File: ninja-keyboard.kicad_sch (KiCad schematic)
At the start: 154 parts, among them J1 USB_C_Receptacle_USB2.0_14P, J2 Conn_01x02, J3 Conn_01x05_Pin, Q1 AO3401A, Q2 SS8050, SW1 backquote, SW10 num9, SW11 num0, SW12 -, SW13 =, SW14 backsapce, SW15 tab, SW16 q, SW17 w, SW18 e, SW19 r, SW2 num1, SW20 t, SW21 y, SW22 u, SW23 i, SW24 o, SW25 p, SW26 [, SW27 ], SW28 \, SW29 cap, SW3 num2, SW30 a, SW31 s, SW32 d, SW33 f, SW34 h, SW35 g, SW36 j, SW37 k, SW38 l, SW39 semicolon, SW4 num3, SW40 apostrophe, SW41 enter, SW42 pgdown, SW43 lshift, SW44 z, SW45 x, SW46 c, SW47 v, SW48 b, SW49 n, SW5 num4, SW50 m, SW51 comma, SW52 period, SW53 /, SW54 rshift, SW55 up, SW56 end, SW57 lctrl, SW58 win, SW59 lalt, SW6 num5, SW60 lfn, SW61 space, SW62 macro, SW63 rfn, SW64 ralt, SW65 rctrl, SW66 left, SW67 down, SW68 right, SW69 pgup, SW7 num6, SW70 home, SW71 RotaryEncoder, SW72 SW_SPDT, SW8 num7, SW9 num8, U1 ESP32-S3-WROOM-1, U3 TP4056-42-ESOP8

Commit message: Seperate capacitors and LEDs from the mechanical keys
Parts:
- added C1, C10, C11, C12, C13, C14, C15, C16, C17, C18, C19, C2, C20, C21, C22, C23, C24, C25, C26, C27, C28, C29, C3, C30, C31, C32, C33, C34, C35, C36, C37, C38, C39, C4, C40, C41, C42, C43, C44, C45, C46, C47, C48, C49, C5, C50, C51, C52, C53, C54, C55, C56, C57, C58, C59, C6, C60, C61, C62, C63, C64, C65, C66, C67, C68, C69, C7, C70, C8, C9: 0.1uF, Capacitor_SMD:C_0603_1608Metric, symbol Device:C_Small
- added SL1, SL10, SL11, SL12, SL13, SL14, SL15, SL16, SL17, SL18, SL19, SL2, SL20, SL21, SL22, SL23, SL24, SL25, SL26, SL27, SL28, SL29, SL3, SL30, SL31, SL32, SL33, SL34, SL35, SL36, SL37, SL38, SL39, SL4, SL40, SL41, SL42, SL43, SL44, SL45, SL46, SL47, SL48, SL49, SL5, SL50, SL51, SL52, SL53, SL54, SL55, SL56, SL57, SL58, SL59, SL6, SL60, SL61, SL62, SL63, SL64, SL65, SL66, SL67, SL68, SL69, SL7, SL70, SL8, SL9: Smart LED, user_added:Smart LED 6028, symbol user_created:Smart LED
- SW1, SW10, SW11, SW12, SW13, SW16, SW17, SW18, SW19, SW2, SW20, SW21, SW22, SW23, SW24, SW25, SW26, SW27, SW3, SW30, SW31, SW32, SW33, SW34, SW35, SW36, SW37, SW38, SW39, SW4, SW40, SW42, SW44, SW45, SW46, SW47, SW48, SW49, SW5, SW50, SW51, SW52, SW53, SW55, SW56, SW6, SW60, SW63, SW66, SW67, SW68, SW69, SW7, SW70, SW8, SW9: footprint user_added:SW_Hotswap_Kailh_MX_1.00u with led -> PCM_Switch_Keyboard_Hotswap_Kailh:SW_Hotswap_Kailh_MX_1.00u; symbol user_created:SW_Push with Smart LED -> Switch:SW_Push
- SW14, SW29: footprint user_added:SW_Hotswap_Kailh_MX_1.75u with led -> PCM_Switch_Keyboard_Hotswap_Kailh:SW_Hotswap_Kailh_MX_1.75u; symbol user_created:SW_Push with Smart LED -> Switch:SW_Push
- SW15: footprint user_added:SW_Hotswap_Kailh_MX_1.50u with led -> PCM_Switch_Keyboard_Hotswap_Kailh:SW_Hotswap_Kailh_MX_1.50u; symbol user_created:SW_Push with Smart LED -> Switch:SW_Push
- SW28, SW57, SW58, SW59, SW64, SW65: footprint user_added:SW_Hotswap_Kailh_MX_1.25u with led -> PCM_Switch_Keyboard_Hotswap_Kailh:SW_Hotswap_Kailh_MX_1.25u; symbol user_created:SW_Push with Smart LED -> Switch:SW_Push
- SW41: footprint user_added:SW_Hotswap_Kailh_MX_2.00u with led -> PCM_Switch_Keyboard_Hotswap_Kailh:SW_Hotswap_Kailh_MX_2.00u; symbol user_created:SW_Push with Smart LED -> Switch:SW_Push
- SW43, SW61, SW62: footprint user_added:SW_Hotswap_Kailh_MX_2.25u with led -> PCM_Switch_Keyboard_Hotswap_Kailh:SW_Hotswap_Kailh_MX_2.25u; symbol user_created:SW_Push with Smart LED -> Switch:SW_Push
- SW54: footprint user_added:SW_Hotswap_Kailh_MX_1.50u with led -> PCM_Switch_Keyboard_Hotswap_Kailh:SW_Hotswap_Kailh_MX_1.00u; symbol user_created:SW_Push with Smart LED -> Switch:SW_Push
- renumbered C3 to C71, C4 to C72, C11 to C73, C5 to C74, C1 to C75, C2 to C76, C6 to C77, C7 to C78, C8 to C79, C9 to C80, C10 to C81, D38 to D36, D36 to D37, D37 to D38, J3 to J1, J4 to J2, J1 to J3, J2 to J4, Q2 to Q1, Q1 to Q2, R18 to R1, R9 to R11, R11 to R12, R12 to R13, R6 to R14, R3 to R15, R4 to R16, R8 to R17, R5 to R18, R14 to R19, R21 to R2, R16 to R20, R15 to R21, R17 to R22, R13 to R23, R1 to R3, R22 to R4, R23 to R5, R7 to R6, R2 to R7, R19 to R8, R20 to R9, U3 to U2, U2 to U3
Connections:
- net 3V3: now also C1.1, C10.1, C11.1, C12.1, C13.1, C14.1, C15.1, C16.1, C17.1, C18.1, C19.1, C2.1, C20.1, C21.1, C22.1, C23.1, C24.1, C25.1, C26.1, C27.1, C28.1, C29.1, C3.1, C30.1, C31.1, C32.1, C33.1, C34.1, C35.1, C36.1, C37.1, C38.1, C39.1, C4.1, C40.1, C41.1, C42.1, C43.1, C44.1, C45.1, C46.1, C47.1, C48.1, C49.1, C5.1, C50.1, C51.1, C52.1, C53.1, C54.1, C55.1, C56.1, C57.1, C58.1, C59.1, C6.1, C60.1, C61.1, C62.1, C63.1, C64.1, C65.1, C66.1, C67.1, C68.1, C69.1, C7.1, C70.1, C8.1, C9.1, SL1.1 (VDD), SL10.1 (VDD), SL11.1 (VDD), SL12.1 (VDD), SL13.1 (VDD), SL14.1 (VDD), SL15.1 (VDD), SL16.1 (VDD), SL17.1 (VDD), SL18.1 (VDD), SL19.1 (VDD), SL2.1 (VDD), SL20.1 (VDD), SL21.1 (VDD), SL22.1 (VDD), SL23.1 (VDD), SL24.1 (VDD), SL25.1 (VDD), SL26.1 (VDD), SL27.1 (VDD), SL28.1 (VDD), SL29.1 (VDD), SL3.1 (VDD), SL30.1 (VDD), SL31.1 (VDD), SL32.1 (VDD), SL33.1 (VDD), SL34.1 (VDD), SL35.1 (VDD), SL36.1 (VDD), SL37.1 (VDD), SL38.1 (VDD), SL39.1 (VDD), SL4.1 (VDD), SL40.1 (VDD), SL41.1 (VDD), SL42.1 (VDD), SL43.1 (VDD), SL44.1 (VDD), SL45.1 (VDD), SL46.1 (VDD), SL47.1 (VDD), SL48.1 (VDD), SL49.1 (VDD), SL5.1 (VDD), SL50.1 (VDD), SL51.1 (VDD), SL52.1 (VDD), SL53.1 (VDD), SL54.1 (VDD), SL55.1 (VDD), SL56.1 (VDD), SL57.1 (VDD), SL58.1 (VDD), SL59.1 (VDD), SL6.1 (VDD), SL60.1 (VDD), SL61.1 (VDD), SL62.1 (VDD), SL63.1 (VDD), SL64.1 (VDD), SL65.1 (VDD), SL66.1 (VDD), SL67.1 (VDD), SL68.1 (VDD), SL69.1 (VDD), SL7.1 (VDD), SL70.1 (VDD), SL8.1 (VDD), SL9.1 (VDD); no longer SW1.3 (VDD), SW10.3 (VDD), SW11.3 (VDD), SW12.3 (VDD), SW13.3 (VDD), SW14.3 (VDD), SW15.3 (VDD), SW16.3 (VDD), SW17.3 (VDD), SW18.3 (VDD), SW19.3 (VDD), SW2.3 (VDD), SW20.3 (VDD), SW21.3 (VDD), SW22.3 (VDD), SW23.3 (VDD), SW24.3 (VDD), SW25.3 (VDD), SW26.3 (VDD), SW27.3 (VDD), SW28.3 (VDD), SW29.3 (VDD), SW3.3 (VDD), SW30.3 (VDD), SW31.3 (VDD), SW32.3 (VDD), SW33.3 (VDD), SW34.3 (VDD), SW35.3 (VDD), SW36.3 (VDD), SW37.3 (VDD), SW38.3 (VDD), SW39.3 (VDD), SW4.3 (VDD), SW40.3 (VDD), SW41.3 (VDD), SW42.3 (VDD), SW43.3 (VDD), SW44.3 (VDD), SW45.3 (VDD), SW46.3 (VDD), SW47.3 (VDD), SW48.3 (VDD), SW49.3 (VDD), SW5.3 (VDD), SW50.3 (VDD), SW51.3 (VDD), SW52.3 (VDD), SW53.3 (VDD), SW54.3 (VDD), SW55.3 (VDD), SW56.3 (VDD), SW57.3 (VDD), SW58.3 (VDD), SW59.3 (VDD), SW6.3 (VDD), SW60.3 (VDD), SW61.3 (VDD), SW62.3 (VDD), SW63.3 (VDD), SW64.3 (VDD), SW65.3 (VDD), SW66.3 (VDD), SW67.3 (VDD), SW68.3 (VDD), SW69.3 (VDD), SW7.3 (VDD), SW70.3 (VDD), SW8.3 (VDD), SW9.3 (VDD)
- net GND: now also C1.2, C10.2, C11.2, C12.2, C13.2, C14.2, C15.2, C16.2, C17.2, C18.2, C19.2, C2.2, C20.2, C21.2, C22.2, C23.2, C24.2, C25.2, C26.2, C27.2, C28.2, C29.2, C3.2, C30.2, C31.2, C32.2, C33.2, C34.2, C35.2, C36.2, C37.2, C38.2, C39.2, C4.2, C40.2, C41.2, C42.2, C43.2, C44.2, C45.2, C46.2, C47.2, C48.2, C49.2, C5.2, C50.2, C51.2, C52.2, C53.2, C54.2, C55.2, C56.2, C57.2, C58.2, C59.2, C6.2, C60.2, C61.2, C62.2, C63.2, C64.2, C65.2, C66.2, C67.2, C68.2, C69.2, C7.2, C70.2, C8.2, C9.2, SL1.4 (GND), SL10.4 (GND), SL11.4 (GND), SL12.4 (GND), SL13.4 (GND), SL14.4 (GND), SL15.4 (GND), SL16.4 (GND), SL17.4 (GND), SL18.4 (GND), SL19.4 (GND), SL2.4 (GND), SL20.4 (GND), SL21.4 (GND), SL22.4 (GND), SL23.4 (GND), SL24.4 (GND), SL25.4 (GND), SL26.4 (GND), SL27.4 (GND), SL28.4 (GND), SL29.4 (GND), SL3.4 (GND), SL30.4 (GND), SL31.4 (GND), SL32.4 (GND), SL33.4 (GND), SL34.4 (GND), SL35.4 (GND), SL36.4 (GND), SL37.4 (GND), SL38.4 (GND), SL39.4 (GND), SL4.4 (GND), SL40.4 (GND), SL41.4 (GND), SL42.4 (GND), SL43.4 (GND), SL44.4 (GND), SL45.4 (GND), SL46.4 (GND), SL47.4 (GND), SL48.4 (GND), SL49.4 (GND), SL5.4 (GND), SL50.4 (GND), SL51.4 (GND), SL52.4 (GND), SL53.4 (GND), SL54.4 (GND), SL55.4 (GND), SL56.4 (GND), SL57.4 (GND), SL58.4 (GND), SL59.4 (GND), SL6.4 (GND), SL60.4 (GND), SL61.4 (GND), SL62.4 (GND), SL63.4 (GND), SL64.4 (GND), SL65.4 (GND), SL66.4 (GND), SL67.4 (GND), SL68.4 (GND), SL69.4 (GND), SL7.4 (GND), SL70.4 (GND), SL8.4 (GND), SL9.4 (GND); no longer SW1.6 (GND), SW10.6 (GND), SW11.6 (GND), SW12.6 (GND), SW13.6 (GND), SW14.6 (GND), SW15.6 (GND), SW16.6 (GND), SW17.6 (GND), SW18.6 (GND), SW19.6 (GND), SW2.6 (GND), SW20.6 (GND), SW21.6 (GND), SW22.6 (GND), SW23.6 (GND), SW24.6 (GND), SW25.6 (GND), SW26.6 (GND), SW27.6 (GND), SW28.6 (GND), SW29.6 (GND), SW3.6 (GND), SW30.6 (GND), SW31.6 (GND), SW32.6 (GND), SW33.6 (GND), SW34.6 (GND), SW35.6 (GND), SW36.6 (GND), SW37.6 (GND), SW38.6 (GND), SW39.6 (GND), SW4.6 (GND), SW40.6 (GND), SW41.6 (GND), SW42.6 (GND), SW43.6 (GND), SW44.6 (GND), SW45.6 (GND), SW46.6 (GND), SW47.6 (GND), SW48.6 (GND), SW49.6 (GND), SW5.6 (GND), SW50.6 (GND), SW51.6 (GND), SW52.6 (GND), SW53.6 (GND), SW54.6 (GND), SW55.6 (GND), SW56.6 (GND), SW57.6 (GND), SW58.6 (GND), SW59.6 (GND), SW6.6 (GND), SW60.6 (GND), SW61.6 (GND), SW62.6 (GND), SW63.6 (GND), SW64.6 (GND), SW65.6 (GND), SW66.6 (GND), SW67.6 (GND), SW68.6 (GND), SW69.6 (GND), SW7.6 (GND), SW70.6 (GND), SW8.6 (GND), SW9.6 (GND)
- net at R1.1: now also SL70.3 (DIN); no longer SW70.5 (DIN)
- new net: SL29.3 (DIN), SL30.2 (DOUT)
- new net: SL30.3 (DIN), SL31.2 (DOUT)
- new net: SL67.3 (DIN), SL68.2 (DOUT)
- new net: SL56.2 (DOUT), SL68.3 (DIN)
- new net: SL12.3 (DIN), SL13.2 (DOUT)
- new net: SL13.3 (DIN), SL14.2 (DOUT)
- new net: SL49.2 (DOUT), SL50.3 (DIN)
- new net: SL48.2 (DOUT), SL49.3 (DIN)
- new net: SL61.3 (DIN), SL62.2 (DOUT)
- new net: SL62.3 (DIN), SL63.2 (DOUT)
- new net: SL57.3 (DIN), SL58.2 (DOUT)
- new net: SL46.2 (DOUT), SL47.3 (DIN)
- new net: SL45.2 (DOUT), SL46.3 (DIN)
- new net: SL15.2 (DOUT), SL16.3 (DIN)
- new net: SL1.2 (DOUT), SL15.3 (DIN)
- new net: SL43.2 (DOUT), SL44.3 (DIN)
- new net: SL29.2 (DOUT), SL43.3 (DIN)
- new net: SL2.3 (DIN), SL3.2 (DOUT)
- new net: SL3.3 (DIN), SL4.2 (DOUT)
- new net: SL14.3 (DIN), SL70.2 (DOUT)
- new net: SL63.3 (DIN), SL64.2 (DOUT)
- new net: SL64.3 (DIN), SL65.2 (DOUT)
- new net: SL38.3 (DIN), SL39.2 (DOUT)
- new net: SL39.3 (DIN), SL40.2 (DOUT)
- new net: SL52.2 (DOUT), SL53.3 (DIN)
- new net: SL51.2 (DOUT), SL52.3 (DIN)
- new net: SL47.2 (DOUT), SL48.3 (DIN)
- new net: SL11.3 (DIN), SL12.2 (DOUT)
- new net: SL58.3 (DIN), SL59.2 (DOUT)
- new net: SL50.2 (DOUT), SL51.3 (DIN)
- new net: SL7.3 (DIN), SL8.2 (DOUT)
- new net: SL8.3 (DIN), SL9.2 (DOUT)
- new net: SL44.2 (DOUT), SL45.3 (DIN)
- new net: SL65.3 (DIN), SL66.2 (DOUT)
- new net: SL66.3 (DIN), SL67.2 (DOUT)
- new net: SL1.3 (DIN), SL2.2 (DOUT)
- new net: SL28.2 (DOUT), SL69.3 (DIN)
- new net: SL27.2 (DOUT), SL28.3 (DIN)
- new net: SL40.3 (DIN), SL41.2 (DOUT)
- new net: SL16.2 (DOUT), SL17.3 (DIN)
- new net: SL41.3 (DIN), SL42.2 (DOUT)
- new net: SL42.3 (DIN), SL69.2 (DOUT)
- new net: SL22.2 (DOUT), SL23.3 (DIN)
- new net: SL21.2 (DOUT), SL22.3 (DIN)
- new net: SL20.2 (DOUT), SL21.3 (DIN)
- new net: SL36.3 (DIN), SL37.2 (DOUT)
- new net: SL37.3 (DIN), SL38.2 (DOUT)
- new net: SL35.3 (DIN), SL36.2 (DOUT)
- new net: SL4.3 (DIN), SL5.2 (DOUT)
- new net: SL5.3 (DIN), SL6.2 (DOUT)
- new net: SL26.2 (DOUT), SL27.3 (DIN)
- new net: SL34.3 (DIN), SL35.2 (DOUT)
- new net: SL6.3 (DIN), SL7.2 (DOUT)
- new net: SL53.2 (DOUT), SL54.3 (DIN)
- new net: SL54.2 (DOUT), SL55.3 (DIN)
- new net: SL33.3 (DIN), SL34.2 (DOUT)
- new net: SL25.2 (DOUT), SL26.3 (DIN)
- new net: SL24.2 (DOUT), SL25.3 (DIN)
- new net: SL10.3 (DIN), SL11.2 (DOUT)
- new net: SL19.2 (DOUT), SL20.3 (DIN)
- new net: SL31.3 (DIN), SL32.2 (DOUT)
- new net: SL18.2 (DOUT), SL19.3 (DIN)
- new net: SL17.2 (DOUT), SL18.3 (DIN)
- new net: SL10.2 (DOUT), SL9.3 (DIN)
- new net: SL23.2 (DOUT), SL24.3 (DIN)
- new net: SL55.2 (DOUT), SL56.3 (DIN)
- new net: SL32.3 (DIN), SL33.2 (DOUT)
- new net: SL59.3 (DIN), SL60.2 (DOUT)
- new net: SL60.3 (DIN), SL61.2 (DOUT)

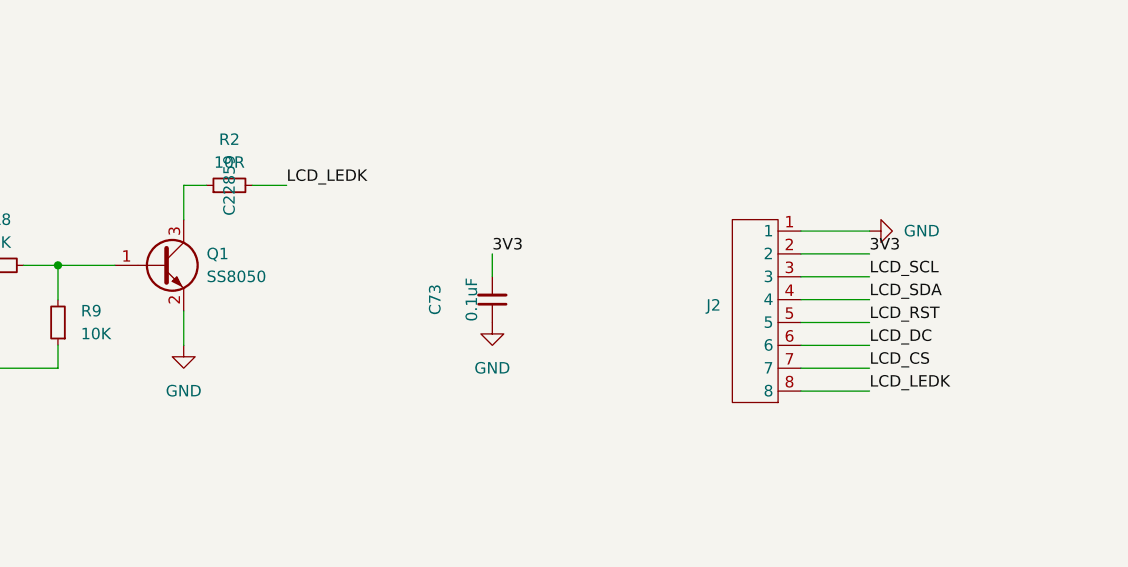
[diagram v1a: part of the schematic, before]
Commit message: Modify LCD socket pin definition
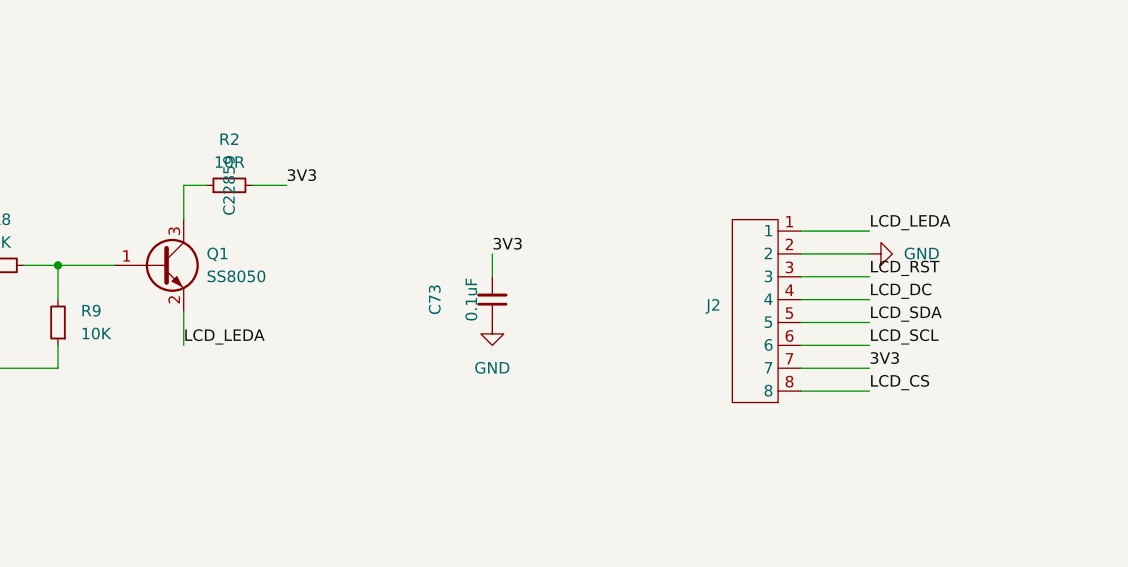
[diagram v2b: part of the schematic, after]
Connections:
- net 3V3: now also J2.7, R2.2; no longer J2.2
- net GND: now also J2.2; no longer J2.1, Q1.2 (E)
- net LCD_CS: now also J2.8; no longer J2.7
- net LCD_DC: now also J2.4; no longer J2.6
- net LCD_RST: now also J2.3; no longer J2.5
- net LCD_SCL: now also J2.6; no longer J2.3
- net LCD_SDA: now also J2.5; no longer J2.4
- removed net LCD_LEDK: J2.8, R2.2
- new net LCD_LEDA: J2.1, Q1.2 (E)
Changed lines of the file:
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@@
 	)
 	(label "LCD_SCL"
-		(at 168.91 245.11 0)
+		(at 168.91 252.73 0)
 		(effects
 			(font
@@
 	)
 	(label "LCD_DC"
-		(at 168.91 252.73 0)
+		(at 168.91 247.65 0)
 		(effects
 			(font
@@
 	)
 	(label "LCD_SDA"
-		(at 168.91 247.65 0)
+		(at 168.91 250.19 0)
 		(effects
 			(font
@@
 	)
 	(label "LCD_RST"
-		(at 168.91 250.19 0)
+		(at 168.91 245.11 0)
 		(effects
 			(font
@@
 		)
 	)
-	(label "LCD_LEDK"
-		(at 104.14 234.95 0)
+	(label "LCD_LEDA"
+		(at 92.71 252.73 0)
 		(effects
 			(font
@@
 	)
 	(label "3V3"
-		(at 168.91 242.57 0)
+		(at 168.91 255.27 0)
 		(effects
 			(font
@@
 	)
 	(label "LCD_CS"
-		(at 168.91 255.27 0)
+		(at 168.91 257.81 0)
 		(effects
 			(font
@@
 	)
 	(label "3V3"
+		(at 104.14 234.95 0)
+		(effects
+			(font
+				(size 1.27 1.27)
+			)
+			(justify left bottom)
+		)
+	)
+	(label "3V3"
 		(at 157.48 85.09 180)
 		(effects
@@
 		)
 	)
-	(label "LCD_LEDK"
-		(at 168.91 257.81 0)
+	(label "LCD_LEDA"
+		(at 168.91 240.03 0)
 		(effects
 			(font
@@
 	(symbol
 		(lib_id "power:GND")
-		(at 92.71 252.73 0)
-		(unit 1)
-		(exclude_from_sim no)
-		(in_bom yes)
-		(on_board yes)
-		(dnp no)
-		(fields_autoplaced yes)
-		(property "Reference" "#PWR0146"
-			(at 92.71 259.08 0)
-			(effects
-				(font
-					(size 1.27 1.27)
-				)
-				(hide yes)
-			)
-		)
-		(property "Value" "GND"
-			(at 92.71 257.81 0)
-			(effects
-				(font
-					(size 1.27 1.27)
-				)
-			)
-		)
-		(property "Footprint" ""
-			(at 92.71 252.73 0)
-			(effects
-				(font
-					(size 1.27 1.27)
-				)
-				(hide yes)
-			)
-		)
-		(property "Datasheet" ""
-			(at 92.71 252.73 0)
-			(effects
-				(font
-					(size 1.27 1.27)
-				)
-				(hide yes)
-			)
-		)
-		(property "Description" "Power symbol creates a global label with name \"GND\" , ground"
-			(at 92.71 252.73 0)
-			(effects
-				(font
-					(size 1.27 1.27)
-				)
-				(hide yes)
-			)
-		)
-		(pin "1"
-		)
-		(instances
-			(project "ninja-keyboard"
-				(path "/38993bca-db6c-4f9a-9477-49e0546421f5"
-					(reference "#PWR0146")
-					(unit 1)
-				)
-			)
-		)
-	)
-	(symbol
-		(lib_id "power:GND")
 		(at 356.87 60.96 0)
 		(unit 1)
@@
 	(symbol
 		(lib_id "power:GND")
-		(at 168.91 240.03 90)
+		(at 168.91 242.57 90)
 		(unit 1)
 		(exclude_from_sim no)
@@
 		(fields_autoplaced yes)
 		(property "Reference" "#PWR0142"
-			(at 175.26 240.03 0)
+			(at 175.26 242.57 0)
 			(effects
 				(font
@@
 		)
 		(property "Value" "GND"
-			(at 172.72 240.0299 90)
+			(at 172.72 242.5699 90)
 			(effects
 				(font
@@
 		)
 		(property "Footprint" ""
-			(at 168.91 240.03 0)
+			(at 168.91 242.57 0)
 			(effects
 				(font
@@
 		)
 		(property "Datasheet" ""
-			(at 168.91 240.03 0)
+			(at 168.91 242.57 0)
 			(effects
 				(font
@@
 		)
 		(property "Description" "Power symbol creates a global label with name \"GND\" , ground"
-			(at 168.91 240.03 0)
+			(at 168.91 242.57 0)
 			(effects
 				(font

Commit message: Add JLC component serial numbers
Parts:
- J1, SW71, U3: now left out of the parts list
- J2: LCSC Part # (none) -> C22370919
- R10: value 4.87K -> 3.9K; LCSC Part # C23045 -> C23018
- R12: value 47.5K -> 30K; LCSC Part # C23061 -> C22984
- SL1, SL10, SL11, SL12, SL13, SL14, SL15, SL16, SL17, SL18, SL19, SL2, SL20, SL21, SL22, SL23, SL24, SL25, SL26, SL27, SL28, SL29, SL3, SL30, SL31, SL32, SL33, SL34, SL35, SL36, SL37, SL38, SL39, SL4, SL40, SL41, SL42, SL43, SL44, SL45, SL46, SL47, SL48, SL49, SL5, SL50, SL51, SL52, SL53, SL54, SL55, SL56, SL57, SL58, SL59, SL6, SL60, SL61, SL62, SL63, SL64, SL65, SL66, SL67, SL68, SL69, SL7, SL70, SL8, SL9: LCSC Part # (none) -> C9900170687
- SW1, SW10, SW11, SW12, SW13, SW14, SW15, SW16, SW17, SW18, SW19, SW2, SW20, SW21, SW22, SW23, SW24, SW25, SW26, SW27, SW28, SW29, SW3, SW30, SW31, SW32, SW33, SW34, SW35, SW36, SW37, SW38, SW39, SW4, SW40, SW41, SW42, SW43, SW44, SW45, SW46, SW47, SW48, SW49, SW5, SW50, SW51, SW52, SW53, SW54, SW55, SW56, SW57, SW58, SW59, SW6, SW60, SW61, SW62, SW63, SW64, SW65, SW66, SW67, SW68, SW69, SW7, SW70, SW8, SW9: LCSC Part # (none) -> C5333465
- SW72: LCSC Part # (none) -> C221660
- U1: LCSC Part # (none) -> C2980297
- U2: LCSC Part # (none) -> C16581

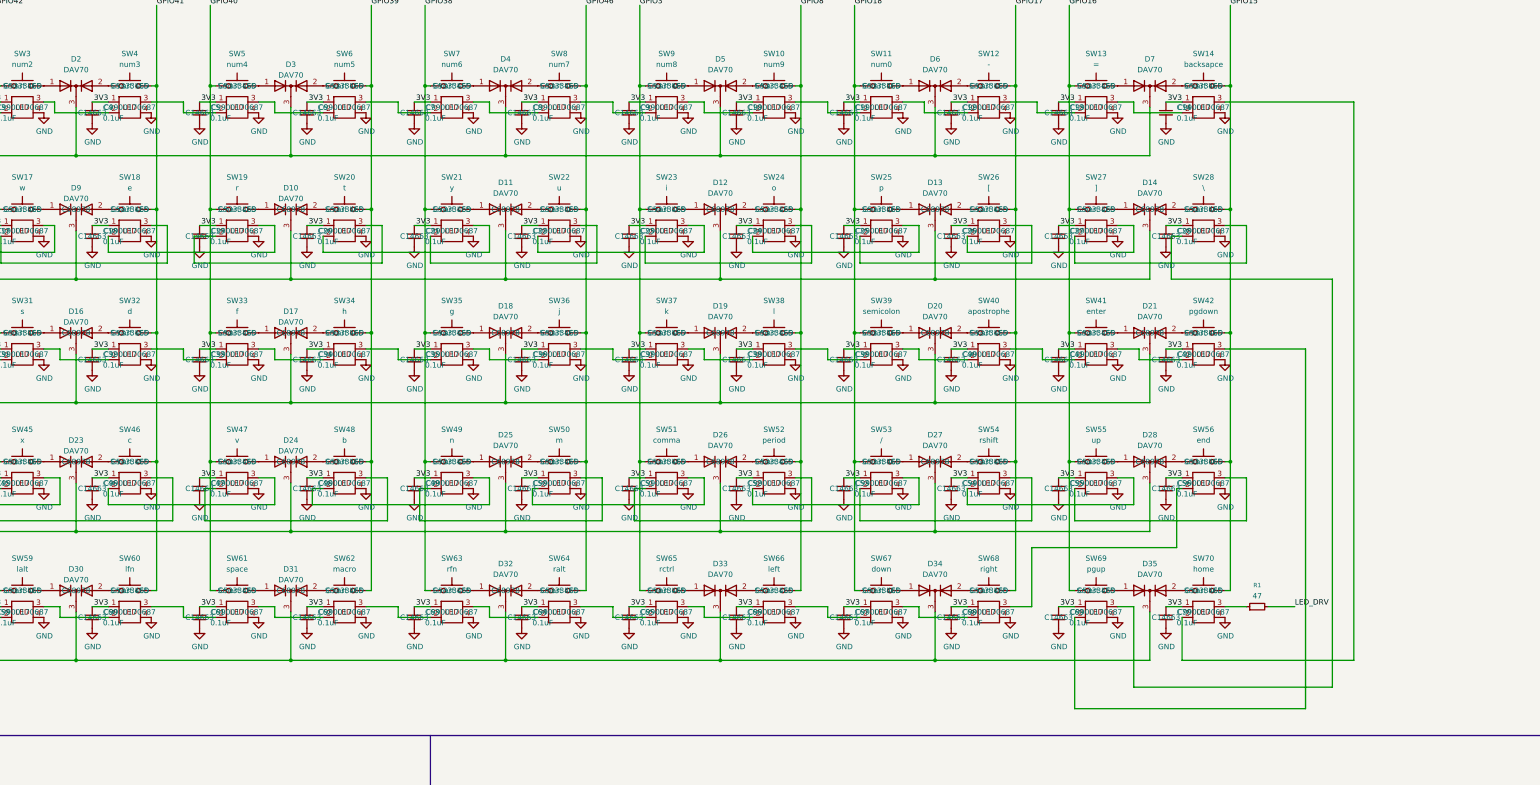
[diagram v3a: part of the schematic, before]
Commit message: Change board dimension to default 60% layout
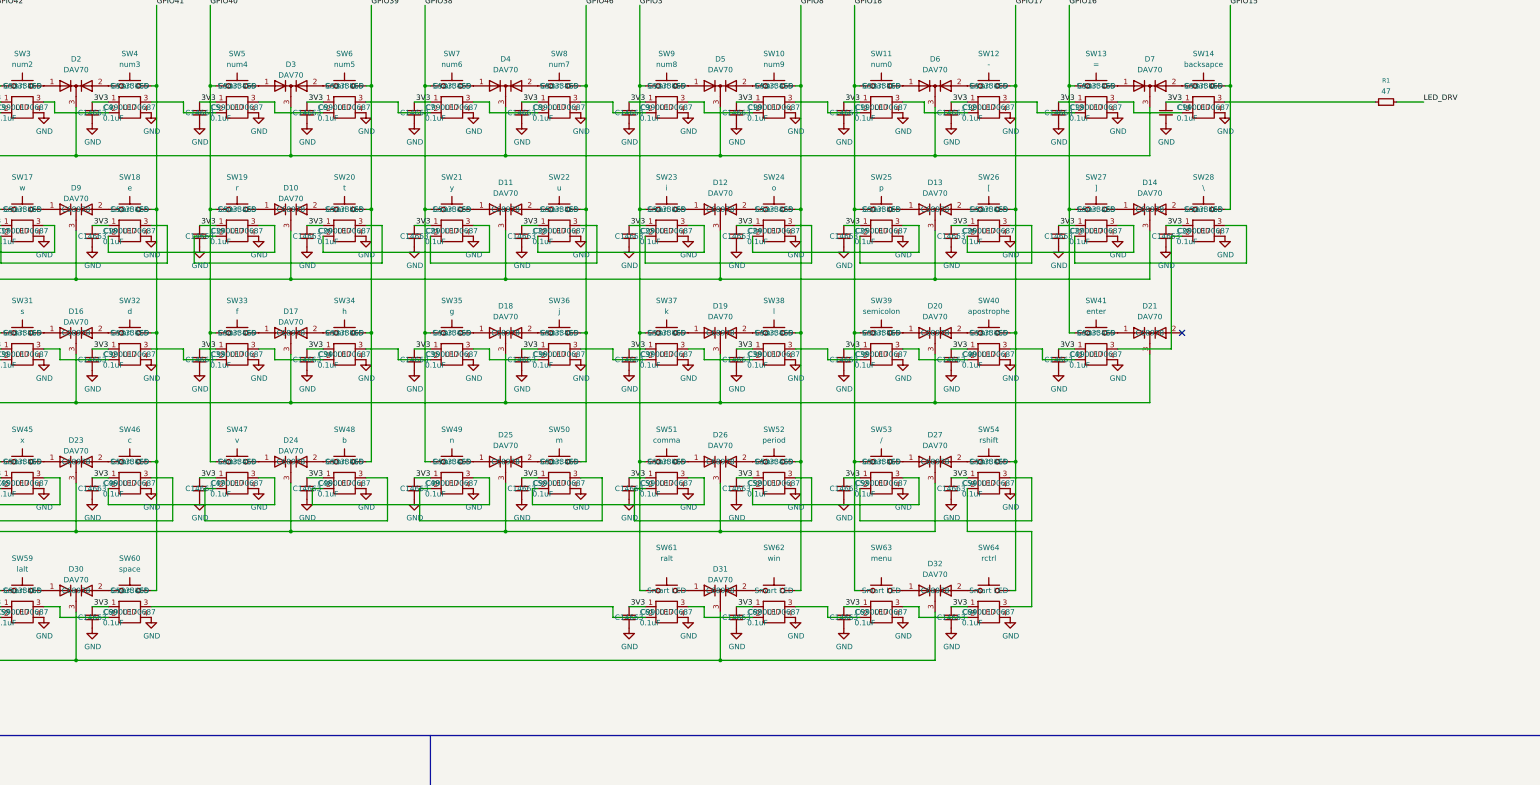
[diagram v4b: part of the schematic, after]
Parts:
- removed C42, C55, C56, C65, C66, C67, C68, C69, C70: 0.1uF, Capacitor_SMD:C_0603_1608Metric, symbol Device:C_Small
- removed D28, D33, D34, D35: DAV70, Package_TO_SOT_SMD:SOT-23, symbol Device:D_Dual_CommonCathode_AAK
- removed SL42, SL55, SL56, SL65, SL66, SL67, SL68, SL69, SL70: Smart LED, user_added:Smart LED 6028, symbol user_created:Smart LED
- removed SW42: pgdown, PCM_Switch_Keyboard_Hotswap_Kailh:SW_Hotswap_Kailh_MX_1.00u, symbol Switch:SW_Push
- removed SW55: up, PCM_Switch_Keyboard_Hotswap_Kailh:SW_Hotswap_Kailh_MX_1.00u, symbol Switch:SW_Push
- removed SW56: end, PCM_Switch_Keyboard_Hotswap_Kailh:SW_Hotswap_Kailh_MX_1.00u, symbol Switch:SW_Push
- removed SW65: rctrl, PCM_Switch_Keyboard_Hotswap_Kailh:SW_Hotswap_Kailh_MX_1.25u, symbol Switch:SW_Push
- removed SW66: left, PCM_Switch_Keyboard_Hotswap_Kailh:SW_Hotswap_Kailh_MX_1.00u, symbol Switch:SW_Push
- removed SW67: down, PCM_Switch_Keyboard_Hotswap_Kailh:SW_Hotswap_Kailh_MX_1.00u, symbol Switch:SW_Push
- removed SW68: right, PCM_Switch_Keyboard_Hotswap_Kailh:SW_Hotswap_Kailh_MX_1.00u, symbol Switch:SW_Push
- removed SW69: pgup, PCM_Switch_Keyboard_Hotswap_Kailh:SW_Hotswap_Kailh_MX_1.00u, symbol Switch:SW_Push
- removed SW70: home, PCM_Switch_Keyboard_Hotswap_Kailh:SW_Hotswap_Kailh_MX_1.00u, symbol Switch:SW_Push
- SW14: footprint PCM_Switch_Keyboard_Hotswap_Kailh:SW_Hotswap_Kailh_MX_1.75u -> PCM_Switch_Keyboard_Hotswap_Kailh:SW_Hotswap_Kailh_MX_2.00u
- SW28: footprint PCM_Switch_Keyboard_Hotswap_Kailh:SW_Hotswap_Kailh_MX_1.25u -> PCM_Switch_Keyboard_Hotswap_Kailh:SW_Hotswap_Kailh_MX_1.50u
- SW41: footprint PCM_Switch_Keyboard_Hotswap_Kailh:SW_Hotswap_Kailh_MX_2.00u -> PCM_Switch_Keyboard_Hotswap_Kailh:SW_Hotswap_Kailh_MX_2.25u
- SW54: footprint PCM_Switch_Keyboard_Hotswap_Kailh:SW_Hotswap_Kailh_MX_1.00u -> PCM_Switch_Keyboard_Hotswap_Kailh:SW_Hotswap_Kailh_MX_2.75u
- SW60: value lfn -> space; footprint PCM_Switch_Keyboard_Hotswap_Kailh:SW_Hotswap_Kailh_MX_1.00u -> PCM_Switch_Keyboard_Hotswap_Kailh:SW_Hotswap_Kailh_MX_6.25u
- SW61: value space -> ralt; footprint PCM_Switch_Keyboard_Hotswap_Kailh:SW_Hotswap_Kailh_MX_2.25u -> PCM_Switch_Keyboard_Hotswap_Kailh:SW_Hotswap_Kailh_MX_1.25u
- SW62: value macro -> win; footprint PCM_Switch_Keyboard_Hotswap_Kailh:SW_Hotswap_Kailh_MX_2.25u -> PCM_Switch_Keyboard_Hotswap_Kailh:SW_Hotswap_Kailh_MX_1.25u
- SW63: value rfn -> menu; footprint PCM_Switch_Keyboard_Hotswap_Kailh:SW_Hotswap_Kailh_MX_1.00u -> PCM_Switch_Keyboard_Hotswap_Kailh:SW_Hotswap_Kailh_MX_1.25u
- SW64: value ralt -> rctrl
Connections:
- net GPIO17: now also SW64.2
- net GPIO18: now also SW63.1
- net GPIO3: now also SW61.1
- net GPIO38: no longer SW63.1
- net GPIO39: no longer SW62.2
- net GPIO40: no longer SW61.1
- net GPIO46: no longer SW64.2
- net GPIO8: now also SW62.2
- net at R1.1: now also SL14.3 (DIN)
- net at SL64.3 (DIN): now also SL54.2 (DOUT)
- net at SL28.2 (DOUT): now also SL41.3 (DIN)
- no-connect marks 3 -> 4
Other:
- moved on the sheet: C61, C62, C63, C64, D31, D32, R1, SW61, SW62, SW63, SW64

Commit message: 1. Widen tracks for smart leds. 2. Increase output pins for smart leds. 3. Use EC11 for knob switch
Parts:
- added R24, R25: 47, Resistor_SMD:R_0603_1608Metric, symbol Device:R_Small
- SW62: renamed from SW71; footprint Rotary_Encoder:RotaryEncoder_Alps_EC12E_Vertical_H20mm -> Rotary_Encoder:RotaryEncoder_Alps_EC12E-Switch_Vertical_H20mm; symbol Device:RotaryEncoder -> Device:RotaryEncoder_Switch_MP; now in the parts list
- renumbered C43 to C42, C44 to C43, C45 to C44, C46 to C45, C47 to C46, C48 to C47, C49 to C48, C50 to C49, C51 to C50, C52 to C51, C53 to C52, C54 to C53, C57 to C54, C58 to C55, C59 to C56, C60 to C57, C61 to C58, C62 to C59, C63 to C60, C64 to C61, C71 to C62, C72 to C63, C73 to C64, C74 to C65, C75 to C66, C76 to C67, C77 to C68, C78 to C69, C79 to C70, C80 to C71, C81 to C72, D29 to D28, D30 to D29, D31 to D30, D32 to D31, D36 to D32, D37 to D33, D38 to D34, D39 to D35, SL43 to SL42, SL44 to SL43, SL45 to SL44, SL46 to SL45, SL47 to SL46, SL48 to SL47, SL49 to SL48, SL50 to SL49, SL51 to SL50, SL52 to SL51, SL53 to SL52, SL54 to SL53, SL57 to SL54, SL58 to SL55, SL59 to SL56, SL60 to SL57, SL61 to SL58, SL62 to SL59, SL63 to SL60, SL64 to SL61, SW43 to SW42, SW44 to SW43, SW45 to SW44, SW46 to SW45, SW47 to SW46, SW48 to SW47, SW49 to SW48, SW50 to SW49, SW51 to SW50, SW52 to SW51, SW53 to SW52, SW54 to SW53, SW57 to SW54, SW58 to SW55, SW59 to SW56, SW60 to SW57, SW61 to SW58, SW62 to SW59, SW63 to SW60, SW64 to SW61, SW72 to SW63
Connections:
- net GND: now also SW62.MP, SW62.S2
- net at SL42.3 (DIN): now also R25.2; no longer SL29.2 (DOUT)
- net at SL21.3 (DIN): now also R24.2; no longer SL20.2 (DOUT)
- net GPIO45: now reaches U1.26 (GPIO45)
- net GPIO45: now also SW62.S1
- net LED_DRV renamed LED_DRV0
- net RXD0 renamed LED_DRV1
- net LED_DRV1: now also R24.1
- net TXD0 renamed LED_DRV2
- net LED_DRV2: now also R25.1
- no-connect marks 4 -> 5
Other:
- moved on the sheet: C66, C67, R4, R5
